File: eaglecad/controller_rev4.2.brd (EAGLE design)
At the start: 40 x 29.5 mm, 81 parts, among them U100 STM32L452XX_QFPN48, U101 TCAN330, U200 TPS63070, U300 STSPIN230, U301 TSV991ILT, U302 AS5047P, U400 STSPIN250, U401 TSV991ILT, X101 ABM10-16MHz

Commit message: rev4.2 ready for review
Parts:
- removed TP1, TP2, TP3, TP4: TPTP06R, testpad:TP06R
- moved C406 23.7 mm to (29.2, 11.3), turned to 90 degrees
- moved R412 22.6 mm to (28.9, 5.97), flipped to the bottom, turned to 270 degrees
- moved R406 21.7 mm to (30.2, 11.3), turned to 90 degrees
- moved R405 21.1 mm to (29.7, 9.82), turned to 180 degrees
- moved C407 19.6 mm to (28.2, 10.9), turned to 270 degrees
- moved R407 19.2 mm to (27.1, 10.3), turned to 90 degrees
- moved R408 17.8 mm to (28.2, 8.77), turned to 90 degrees
- moved R411 17.6 mm to (29.7, 8.73), flipped to the bottom, turned to 180 degrees
- moved R413 10.8 mm to (35.4, 9.25), turned to 270 degrees
- moved C403 9.36 mm to (22.1, 3.08), flipped to the top, turned to 270 degrees
- moved R414 9.35 mm to (34.9, 10.7), turned to 180 degrees
- moved C402 8.86 mm to (23.6, 3.08), flipped to the top, turned to 270 degrees
- moved C401 8.86 mm to (25.1, 3.08), flipped to the top, turned to 270 degrees
- moved C411 8.82 mm to (34.4, 9.25), turned to 90 degrees
- moved R401 6.58 mm to (25.3, 11.5)
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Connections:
- removed net V_BATT: U$1.VCC1, U$1.VCC2, U$1.VCC3, U$1.VCC4
- net BLDC_STBY: no longer TP2.TP
- net BOOT: no longer TP4.TP
- net CAN_SHDN: no longer TP1.TP
- net MAG_STBY: no longer TP3.TP
- net OUT1: now also U$1.MAG1; no longer U$1.MAG2
- net OUT2: now also U$1.MAG2; no longer U$1.MAG1
- net VBUS: now also U$1.VCC1, U$1.VCC2, U$1.VCC3, U$1.VCC4
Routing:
- net GND: track 35.9 -> 63.4 mm, vias 152 -> 177
- net I2C_SCL: track 0.00 -> 24.5 mm, vias 0 -> 1
- net I2C_SDA: track 0.00 -> 22.6 mm, vias 0 -> 1
- net BOOT: track 1.32 -> 15.8 mm, vias 0 -> 1
- net OUT1: track 0.00 -> 10.8 mm, vias 0 -> 2
- net CAN_RX: track 3.93 -> 13.8 mm
- net CAN_TX: track 3.43 -> 12.3 mm
- net CAN_SILENT: track 9.34 -> 18.2 mm
- net SENSE_MAG: track 1.81 -> 10.4 mm, vias 0 -> 2
- net VBUS: track 6.58 -> 13.9 mm, vias 10 -> 19
- net MAG_FAULT: track 3.43 -> 9.32 mm
- net OUT2: track 0.01 -> 5.89 mm, vias 0 -> 2
- net MAG_PWM: track 0.00 -> 5.39 mm, vias 0 -> 2
- net MAG_DIR: track 0.00 -> 5.28 mm, vias 0 -> 2
- net CAN_H: track 0.00 -> 4.77 mm, vias 0 -> 1
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
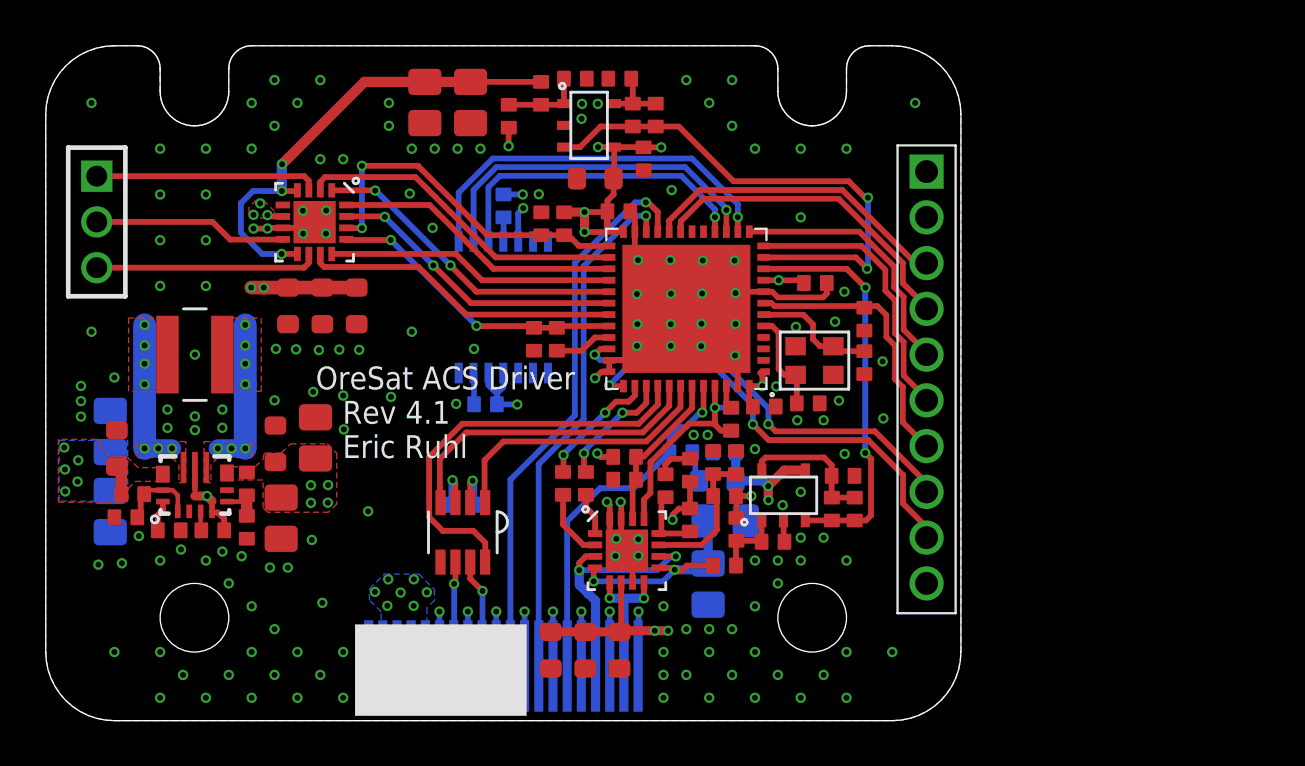
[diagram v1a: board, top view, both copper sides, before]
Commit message: added quadrent marker resistors and tappered lower corners for more clearence
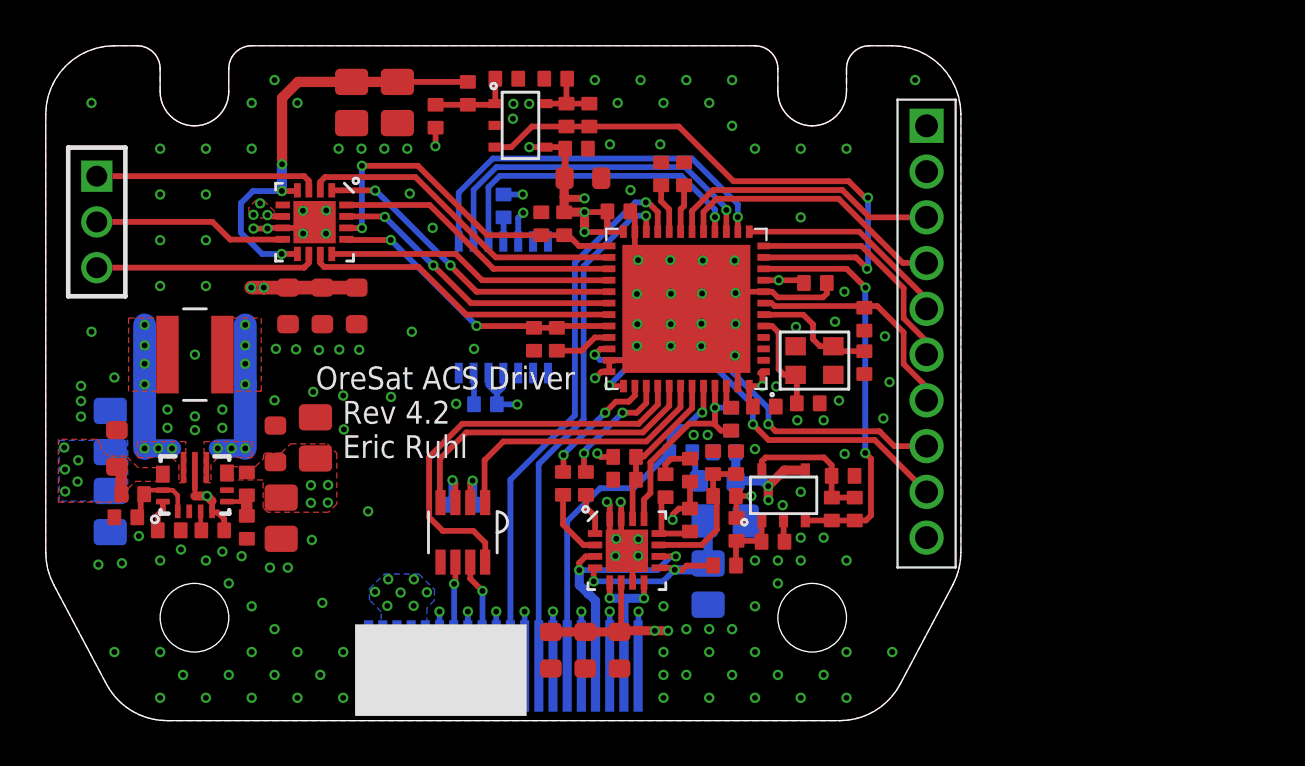
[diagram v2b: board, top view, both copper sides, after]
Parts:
- added R102, R103: 0, rcl_custom:.0402-B-NOSILK
- moved R305 3.20 mm to (13.4, 27.0)
- moved R306 3.20 mm to (15.4, 27.0)
- moved R303 3.20 mm to (17.0, 26.4)
- moved R304 3.20 mm to (18.4, 27.4)
- moved C308 3.00 mm to (20.1, 28.1)
- moved U301 3.00 mm to (20.8, 26.0)
- moved C307 2.96 mm to (23.2, 25.0), turned to 0 degrees
- moved C309 2.90 mm to (23.8, 26.5)
- moved R307 2.90 mm to (22.8, 26.5)
- moved R308 2.80 mm to (22.3, 28.1)
- moved C501 2.00 mm to (38.5, 18.0)
- moved C306 0.54 mm to (23.5, 23.7), turned to 0 degrees
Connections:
- new net ADDR_0: R102.2, U100.19
- new net ADDR_1: R103.2, U100.20
- net DEBUG_1: now also U100.18; no longer U100.20
- net DEBUG_2: now also U100.17; no longer U100.19
- net GND: now also R102.1, R103.1
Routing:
- net BLDC_CURR_FDB: track 22.8 -> 25.8 mm
- net ADDR_1: track 0.00 -> 2.17 mm
- net DEBUG_2: track 14.2 -> 12.0 mm
- net ADDR_0: track 0.00 -> 2.09 mm
- net UART_RX: track 11.4 -> 9.34 mm
- net UART_TX: track 12.2 -> 10.2 mm
- net NRST: track 12.3 -> 10.3 mm
- net SWCLK: track 19.4 -> 17.6 mm
- net DEBUG_1: track 13.6 -> 12.0 mm
- net SENSE_BLDC: track 20.8 -> 19.3 mm
- net SWDIO: track 18.4 -> 17.3 mm
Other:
- outline, holes or cut-outs redrawn
- board text added: "OreSat ACS Driver Rev 4.2 Eric Ruhl"
- board text removed: "OreSat ACS Driver Rev 4.1 Eric Ruhl"
